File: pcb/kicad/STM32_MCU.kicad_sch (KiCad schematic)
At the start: 13 parts, among them J2 Conn_ARM_JTAG_SWD_10, SW1 SW_Push, U2 STM32G431K8Tx

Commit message: Add additional test points (and breakouts) for stm32
- Breakouts for 3 additional GPIO pins which can double as a test point
  if needed
- Added test point for GPIO debug which can be seen visually via the
  GPIO debug LED, test point added for possibility of capturing traces
  (needed for timing patches)
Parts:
- added TP56, TP57, TP58, TP59: TestPoint_2Pole, Diode_SMD:D_0402_1005Metric, symbol Connector:TestPoint_2Pole
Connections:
- net GND: now also TP56.2, TP57.2, TP58.2, TP59.2
- net GPIO_DEBUG1: now also TP56.1
- net at U2.10 (PA5): now also TP58.1
- net at U2.11 (PA6): now also TP59.1
- net at U2.5 (PA0): now also TP57.1
- no-connect marks 15 -> 12
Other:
- note added: "Breakout extra GPIO pins via test points"

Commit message: Update bom/mpn attributes
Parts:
- C10: MPN (none) -> GRM188Z71C475KE21D
- C11, C12, C7, C8: MPN (none) -> C0603C104J3RACTU
- C9: MPN (none) -> GCG188L8EE105KA07D
- D4: value LED_Small_Filled -> GPIO Debug LED (GREEN); MPN (none) -> LTST-C190KGKT
- J2: MPN (none) -> FTSH-105-01-L-D-K
- R3: MPN (none) -> RT0603FRE0710RL
- SW1: MPN (none) -> TL3305AF260QG
- TP56, TP57, TP58, TP59: now left out of the parts list
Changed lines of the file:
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@@
 		(unit 1)
 		(exclude_from_sim no)
-		(in_bom yes)
+		(in_bom no)
 		(on_board yes)
 		(dnp no)
@@
 			)
 		)
+		(property "MPN" "GRM188Z71C475KE21D"
+			(at 87.63 151.13 0)
+			(effects
+				(font
+					(size 1.27 1.27)
+				)
+				(hide yes)
+			)
+		)
 		(pin "2"
 		)
@@
 		)
 		(property "Description" "Unpolarized capacitor"
+			(at 53.34 151.13 0)
+			(effects
+				(font
+					(size 1.27 1.27)
+				)
+				(hide yes)
+			)
+		)
+		(property "MPN" "C0603C104J3RACTU"
 			(at 53.34 151.13 0)
 			(effects
@@
 		(unit 1)
 		(exclude_from_sim no)
-		(in_bom yes)
+		(in_bom no)
 		(on_board yes)
 		(dnp no)
@@
 			)
 		)
+		(property "MPN" "C0603C104J3RACTU"
+			(at 109.22 151.13 0)
+			(effects
+				(font
+					(size 1.27 1.27)
+				)
+				(hide yes)
+			)
+		)
 		(pin "2"
 		)
@@
 			)
 		)
+		(property "MPN" "RT0603FRE0710RL"
+			(at 100.33 106.68 0)
+			(effects
+				(font
+					(size 1.27 1.27)
+				)
+				(hide yes)
+			)
+		)
 		(pin "2"
 		)
@@
 		)
 		(property "Description" "Unpolarized capacitor"
+			(at 97.79 151.13 0)
+			(effects
+				(font
+					(size 1.27 1.27)
+				)
+				(hide yes)
+			)
+		)
+		(property "MPN" "C0603C104J3RACTU"
 			(at 97.79 151.13 0)
 			(effects
@@
 			)
 		)
+		(property "MPN" "GCG188L8EE105KA07D"
+			(at 63.5 151.13 0)
+			(effects
+				(font
+					(size 1.27 1.27)
+				)
+				(hide yes)
+			)
+		)
 		(pin "2"
 		)
@@
 			)
 		)
+		(property "MPN" "TL3305AF260QG"
+			(at 64.77 57.15 90)
+			(effects
+				(font
+					(size 1.27 1.27)
+				)
+				(hide yes)
+			)
+		)
 		(pin "1"
 		)
@@
 			)
 		)
-		(property "Value" "LED_Small_Filled"
+		(property "Value" "GPIO Debug LED (GREEN)"
 			(at 161.2265 92.71 0)
 			(effects
@@
 			)
 		)
+		(property "MPN" "LTST-C190KGKT"
+			(at 161.29 96.52 0)
+			(effects
+				(font
+					(size 1.27 1.27)
+				)
+				(hide yes)
+			)
+		)
 		(pin "2"
 		)
@@
 		(unit 1)
 		(exclude_from_sim no)
-		(in_bom yes)
+		(in_bom no)
 		(on_board yes)
 		(dnp no)
@@
 		)
 		(property "Description" "Unpolarized capacitor"
+			(at 76.2 57.15 0)
+			(effects
+				(font
+					(size 1.27 1.27)
+				)
+				(hide yes)
+			)
+		)
+		(property "MPN" "C0603C104J3RACTU"
 			(at 76.2 57.15 0)
 			(effects
@@
 			)
 		)
+		(property "MPN" "FTSH-105-01-L-D-K"
+			(at 213.36 110.49 0)
+			(effects
+				(font
+					(size 1.27 1.27)
+				)
+				(hide yes)
+			)
+		)
 		(pin "6"
 		)
@@
 		(unit 1)
 		(exclude_from_sim no)
-		(in_bom yes)
-		(on_board yes)
-		(dnp no)
+		(in_bom no)
+		(on_board yes)
+		(dnp no)

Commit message: Correct 10k resistor part number
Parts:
- R3: MPN RT0603FRE0710RL -> RT0603FRE0710KL
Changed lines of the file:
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@@
 			)
 		)
-		(property "MPN" "RT0603FRE0710RL"
+		(property "MPN" "RT0603FRE0710KL"
 			(at 100.33 106.68 0)
 			(effects

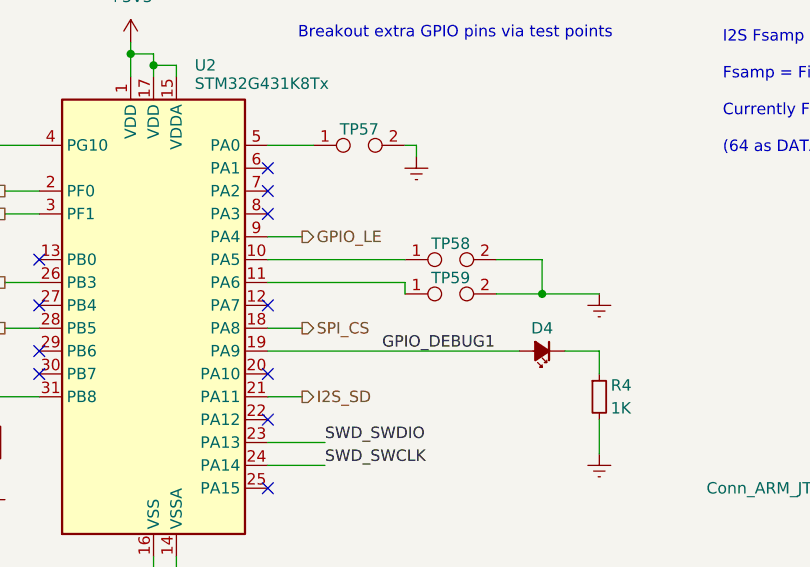
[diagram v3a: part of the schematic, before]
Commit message: Correct stm32 outputs for led driver ic
- SPI CS is analogous to LE, but was instead mapped to OE which in my
  initial tests were tied to GND (all LEDs could be driven)
- Now SPI CS has been renamed to OE and is still mapped to OE pin on the
  STP led driver IC
- GPIO LE is now correctly mapped the LE input on the STP too
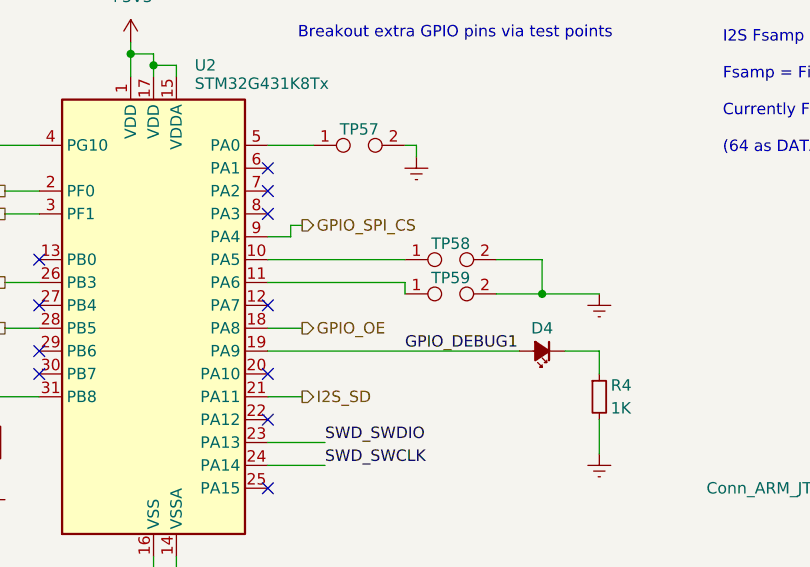
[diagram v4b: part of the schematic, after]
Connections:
- net GPIO_LE renamed GPIO_SPI_CS
- net SPI_CS renamed GPIO_OE
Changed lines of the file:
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@@
 	(title_block
 		(title "STM32G431Kx Schematic")
-		(date "2025-06-29")
-		(rev "v09")
+		(date "2025-11-01")
+		(rev "v10")
 		(comment 1 "No ADC therefore tying VDDA to VDD and GNDA to GND")
 		(comment 2 "Decoupling capacitor info can be found on datasheet and application note AN5093 ")
@@
 	(wire
 		(pts
+			(xy 130.81 93.98) (xy 134.62 93.98)
+		)
+		(stroke
+			(width 0)
+			(type default)
+		)
+	)
+	(wire
+		(pts
 			(xy 226.06 110.49) (xy 246.38 110.49)
 		)
@@
 	(wire
 		(pts
-			(xy 130.81 83.82) (xy 134.62 83.82)
+			(xy 133.35 82.55) (xy 134.62 82.55)
 		)
 		(stroke
@@
 	(wire
 		(pts
+			(xy 133.35 83.82) (xy 130.81 83.82)
+		)
+		(stroke
+			(width 0)
+			(type default)
+		)
+	)
+	(wire
+		(pts
 			(xy 167.64 96.52) (xy 167.64 99.06)
 		)
@@
 	(wire
 		(pts
+			(xy 133.35 82.55) (xy 133.35 83.82)
+		)
+		(stroke
+			(width 0)
+			(type default)
+		)
+	)
+	(wire
+		(pts
 			(xy 87.63 46.99) (xy 76.2 46.99)
 		)
@@
 		(pts
 			(xy 161.29 86.36) (xy 156.21 86.36)
-		)
-		(stroke
-			(width 0)
-			(type default)
-		)
-	)
-	(wire
-		(pts
-			(xy 130.81 93.98) (xy 134.62 93.98)
 		)
 		(stroke
@@
 	)
 	(label "GPIO_DEBUG1"
-		(at 143.51 96.52 0)
+		(at 146.05 96.52 0)
 		(effects
 			(font
@@
 		)
 	)
-	(hierarchical_label "SPI_CS"
+	(hierarchical_label "GPIO_OE"
 		(shape output)
 		(at 134.62 93.98 0)
@@
 		)
 	)
-	(hierarchical_label "GPIO_LE"
+	(hierarchical_label "GPIO_SPI_CS"
 		(shape output)
-		(at 134.62 83.82 0)
-		(effects
-			(font
+		(at 134.62 82.55 0)
+		(effects
+			(font

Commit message: Replace test point footprints
- Quite difficult to probe the 0402 SMD sized test points with my PCBite
  probes
- End up scraping up the PCB trying to probe my test points as the gap
  is too small (on the 0402 footprint)
- The 0805 and microMELF footprints are appropriately sized for hands
  free probing
- Used microMELF footprints where space was very tight (as the microMELF
  occupies a slightly smaller area)
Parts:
- TP56, TP57, TP58, TP59: footprint Diode_SMD:D_0402_1005Metric -> Diode_SMD:D_MicroMELF
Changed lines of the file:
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@@
 			)
 		)
-		(property "Footprint" "Diode_SMD:D_0402_1005Metric"
+		(property "Footprint" "Diode_SMD:D_MicroMELF"
 			(at 151.13 86.36 0)
 			(effects
@@
 			)
 		)
-		(property "Footprint" "Diode_SMD:D_0402_1005Metric"
+		(property "Footprint" "Diode_SMD:D_MicroMELF"
 			(at 153.67 53.34 0)
 			(effects
@@
 			)
 		)
-		(property "Footprint" "Diode_SMD:D_0402_1005Metric"
+		(property "Footprint" "Diode_SMD:D_MicroMELF"
 			(at 140.97 73.66 0)
 			(effects
@@
 			)
 		)
-		(property "Footprint" "Diode_SMD:D_0402_1005Metric"
+		(property "Footprint" "Diode_SMD:D_MicroMELF"
 			(at 151.13 90.17 0)
 			(effects
